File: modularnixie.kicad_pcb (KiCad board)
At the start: 2 copper layers, 69.8 x 21.6 mm, 37 parts, among them J1 Feed, J2 Feed, J3 HV, J4 HV, Q1 MMBT5551, Q10 MMBT5551, Q11 MMBT5551, Q12 MMBT5551, Q13 MMBT5551, Q14 MMBT5551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

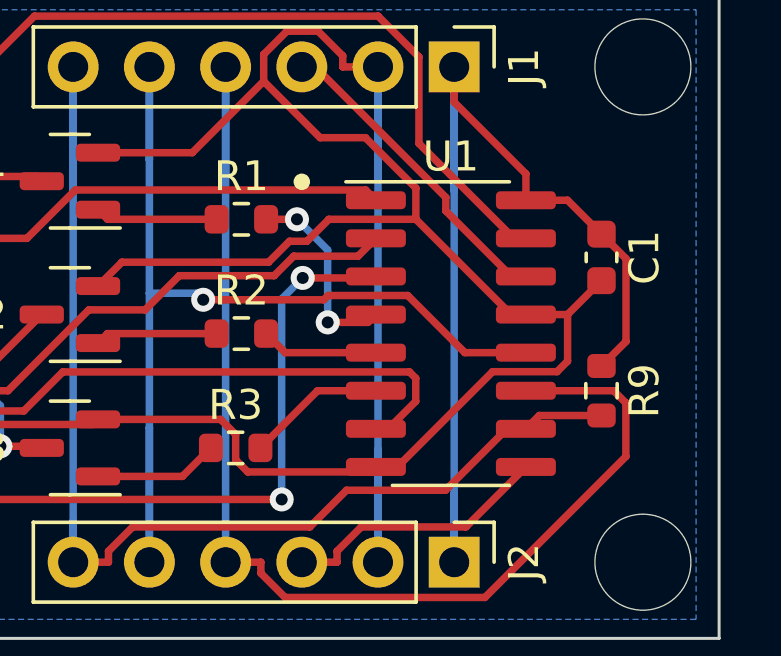
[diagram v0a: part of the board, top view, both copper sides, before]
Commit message: Actually replace SOP-16 with SOIC-16 to get 3D model
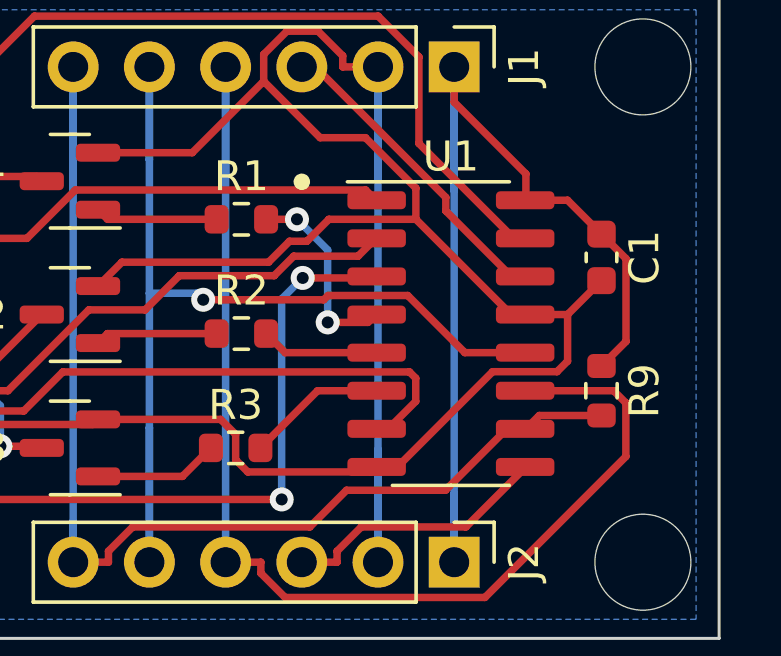
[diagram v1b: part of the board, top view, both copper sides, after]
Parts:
- U1: footprint Package_SO:SOP-16_3.9x9.9mm_P1.27mm -> Package_SO:SOIC-16_3.9x9.9mm_P1.27mm
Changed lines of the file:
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@@
     )
   )
-  (footprint "Package_SO:SOP-16_3.9x9.9mm_P1.27mm" (layer "F.Cu")
+  (footprint "Package_SO:SOIC-16_3.9x9.9mm_P1.27mm" (layer "F.Cu")
     (at 127.7172 64.135)
-    (descr "SOP, 16 Pin (https://www.diodes.com/assets/Datasheets/PAM8403.pdf), generated with kicad-footprint-generator ipc_gullwing_generator.py")
-    (tags "SOP SO")
+    (descr "SOIC, 16 Pin (JEDEC MS-012AC, https://www.analog.com/media/en/package-pcb-resources/package/pkg_pdf/soic_narrow-r/r_16.pdf), generated with kicad-footprint-generator ipc_gullwing_generator.py")
+    (tags "SOIC SO")
     (property "LCSC" "C5947")
     (property "Sheetfile" "modularnixie.kicad_sch")
@@
       (effects (font (size 0.98 0.98) (thickness 0.15)))
     )
+    (fp_line (start 0 -5.06) (end -3.45 -5.06) (layer "F.SilkS") (width 0.12))
+    (fp_line (start 0 5.06) (end 1.95 5.06) (layer "F.SilkS") (width 0.12))
+    (fp_line (start 0 -5.06) (end 1.95 -5.06) (layer "F.SilkS") (width 0.12))
     (fp_line (start 0 5.06) (end -1.95 5.06) (layer "F.SilkS") (width 0.12))
-    (fp_line (start 0 5.06) (end 1.95 5.06) (layer "F.SilkS") (width 0.12))
-    (fp_line (start 0 -5.06) (end -3.5 -5.06) (layer "F.SilkS") (width 0.12))
-    (fp_line (start 0 -5.06) (end 1.95 -5.06) (layer "F.SilkS") (width 0.12))
-    (fp_line (start -3.75 5.2) (end 3.75 5.2) (layer "F.CrtYd") (width 0.05))
-    (fp_line (start -3.75 -5.2) (end -3.75 5.2) (layer "F.CrtYd") (width 0.05))
-    (fp_line (start 3.75 -5.2) (end -3.75 -5.2) (layer "F.CrtYd") (width 0.05))
-    (fp_line (start 3.75 5.2) (end 3.75 -5.2) (layer "F.CrtYd") (width 0.05))
+    (fp_line (start 3.7 5.2) (end 3.7 -5.2) (layer "F.CrtYd") (width 0.05))
+    (fp_line (start -3.7 5.2) (end 3.7 5.2) (layer "F.CrtYd") (width 0.05))
+    (fp_line (start -3.7 -5.2) (end -3.7 5.2) (layer "F.CrtYd") (width 0.05))
+    (fp_line (start 3.7 -5.2) (end -3.7 -5.2) (layer "F.CrtYd") (width 0.05))
+    (fp_line (start 1.95 4.95) (end -1.95 4.95) (layer "F.Fab") (width 0.1))
+    (fp_line (start -0.975 -4.95) (end 1.95 -4.95) (layer "F.Fab") (width 0.1))
+    (fp_line (start -1.95 -3.975) (end -0.975 -4.95) (layer "F.Fab") (width 0.1))
+    (fp_line (start -1.95 4.95) (end -1.95 -3.975) (layer "F.Fab") (width 0.1))
     (fp_line (start 1.95 -4.95) (end 1.95 4.95) (layer "F.Fab") (width 0.1))
-    (fp_line (start -1.95 4.95) (end -1.95 -3.975) (layer "F.Fab") (width 0.1))
-    (fp_line (start -1.95 -3.975) (end -0.975 -4.95) (layer "F.Fab") (width 0.1))
-    (fp_line (start -0.975 -4.95) (end 1.95 -4.95) (layer "F.Fab") (width 0.1))
-    (fp_line (start 1.95 4.95) (end -1.95 4.95) (layer "F.Fab") (width 0.1))
-    (pad "1" smd roundrect (at -2.5 -4.445) (size 2 0.6) (layers "F.Cu" "F.Paste" "F.Mask") (roundrect_rratio 0.25)
+    (pad "1" smd roundrect (at -2.475 -4.445) (size 1.95 0.6) (layers "F.Cu" "F.Paste" "F.Mask") (roundrect_rratio 0.25)
       (net 34 "Net-(R11-Pad2)") (pinfunction "QB") (pintype "tri_state"))
-    (pad "2" smd roundrect (at -2.5 -3.175) (size 2 0.6) (layers "F.Cu" "F.Paste" "F.Mask") (roundrect_rratio 0.25)
+    (pad "2" smd roundrect (at -2.475 -3.175) (size 1.95 0.6) (layers "F.Cu" "F.Paste" "F.Mask") (roundrect_rratio 0.25)
       (net 35 "Net-(R12-Pad2)") (pinfunction "QC") (pintype "tri_state"))
-    (pad "3" smd roundrect (at -2.5 -1.905) (size 2 0.6) (layers "F.Cu" "F.Paste" "F.Mask") (roundrect_rratio 0.25)
+    (pad "3" smd roundrect (at -2.475 -1.905) (size 1.95 0.6) (layers "F.Cu" "F.Paste" "F.Mask") (roundrect_rratio 0.25)
       (net 36 "Net-(R13-Pad2)") (pinfunction "QD") (pintype "tri_state"))
-    (pad "4" smd roundrect (at -2.5 -0.635) (size 2 0.6) (layers "F.Cu" "F.Paste" "F.Mask") (roundrect_rratio 0.25)
+    (pad "4" smd roundrect (at -2.475 -0.635) (size 1.95 0.6) (layers "F.Cu" "F.Paste" "F.Mask") (roundrect_rratio 0.25)
       (net 30 "Net-(R1-Pad2)") (pinfunction "QE") (pintype "tri_state"))
-    (pad "5" smd roundrect (at -2.5 0.635) (size 2 0.6) (layers "F.Cu" "F.Paste" "F.Mask") (roundrect_rratio 0.25)
+    (pad "5" smd roundrect (at -2.475 0.635) (size 1.95 0.6) (layers "F.Cu" "F.Paste" "F.Mask") (roundrect_rratio 0.25)
       (net 31 "Net-(R2-Pad2)") (pinfunction "QF") (pintype "tri_state"))
-    (pad "6" smd roundrect (at -2.5 1.905) (size 2 0.6) (layers "F.Cu" "F.Paste" "F.Mask") (roundrect_rratio 0.25)
+    (pad "6" smd roundrect (at -2.475 1.905) (size 1.95 0.6) (layers "F.Cu" "F.Paste" "F.Mask") (roundrect_rratio 0.25)
       (net 32 "Net-(R3-Pad2)") (pinfunction "QG") (pintype "tri_state"))
-    (pad "7" smd roundrect (at -2.5 3.175) (size 2 0.6) (layers "F.Cu" "F.Paste" "F.Mask") (roundrect_rratio 0.25)
+    (pad "7" smd roundrect (at -2.475 3.175) (size 1.95 0.6) (layers "F.Cu" "F.Paste" "F.Mask") (roundrect_rratio 0.25)
       (net 39 "Net-(R4-Pad2)") (pinfunction "QH") (pintype "tri_state"))
-    (pad "8" smd roundrect (at -2.5 4.445) (size 2 0.6) (layers "F.Cu" "F.Paste" "F.Mask") (roundrect_rratio 0.25)
+    (pad "8" smd roundrect (at -2.475 4.445) (size 1.95 0.6) (layers "F.Cu" "F.Paste" "F.Mask") (roundrect_rratio 0.25)
       (net 2 "GND") (pinfunction "GND") (pintype "power_in"))
-    (pad "9" smd roundrect (at 2.5 4.445) (size 2 0.6) (layers "F.Cu" "F.Paste" "F.Mask") (roundrect_rratio 0.25)
+    (pad "9" smd roundrect (at 2.475 4.445) (size 1.95 0.6) (layers "F.Cu" "F.Paste" "F.Mask") (roundrect_rratio 0.25)
       (net 7 "Net-(J2-Pad3)") (pinfunction "QH'") (pintype "output"))
-    (pad "10" smd roundrect (at 2.5 3.175) (size 2 0.6) (layers "F.Cu" "F.Paste" "F.Mask") (roundrect_rratio 0.25)
+    (pad "10" smd roundrect (at 2.475 3.175) (size 1.95 0.6) (layers "F.Cu" "F.Paste" "F.Mask") (roundrect_rratio 0.25)
       (net 3 "Net-(J1-Pad6)") (pinfunction "~{SRCLR}") (pintype "input"))
-    (pad "11" smd roundrect (at 2.5 1.905) (size 2 0.6) (layers "F.Cu" "F.Paste" "F.Mask") (roundrect_rratio 0.25)
+    (pad "11" smd roundrect (at 2.475 1.905) (size 1.95 0.6) (layers "F.Cu" "F.Paste" "F.Mask") (roundrect_rratio 0.25)
       (net 5 "Net-(J1-Pad4)") (pinfunction "SRCLK") (pintype "input"))
-    (pad "12" smd roundrect (at 2.5 0.635) (size 2 0.6) (layers "F.Cu" "F.Paste" "F.Mask") (roundrect_rratio 0.25)
+    (pad "12" smd roundrect (at 2.475 0.635) (size 1.95 0.6) (layers "F.Cu" "F.Paste" "F.Mask") (roundrect_rratio 0.25)
       (net 6 "Net-(J1-Pad5)") (pinfunction "RCLK") (pintype "input"))
-    (pad "13" smd roundrect (at 2.5 -0.635) (size 2 0.6) (layers "F.Cu" "F.Paste" "F.Mask") (roundrect_rratio 0.25)
+    (pad "13" smd roundrect (at 2.475 -0.635) (size 1.95 0.6) (layers "F.Cu" "F.Paste" "F.Mask") (roundrect_rratio 0.25)
       (net 2 "GND") (pinfunction "~{OE}") (pintype "input"))
-    (pad "14" smd roundrect (at 2.5 -1.905) (size 2 0.6) (layers "F.Cu" "F.Paste" "F.Mask") (roundrect_rratio 0.25)
+    (pad "14" smd roundrect (at 2.475 -1.905) (size 1.95 0.6) (layers "F.Cu" "F.Paste" "F.Mask") (roundrect_rratio 0.25)
       (net 4 "Net-(J1-Pad3)") (pinfunction "SER") (pintype "input"))
-    (pad "15" smd roundrect (at 2.5 -3.175) (size 2 0.6) (layers "F.Cu" "F.Paste" "F.Mask") (roundrect_rratio 0.25)
+    (pad "15" smd roundrect (at 2.475 -3.175) (size 1.95 0.6) (layers "F.Cu" "F.Paste" "F.Mask") (roundrect_rratio 0.25)
       (net 33 "Net-(R10-Pad2)") (pinfunction "QA") (pintype "tri_state"))
-    (pad "16" smd roundrect (at 2.5 -4.445) (size 2 0.6) (layers "F.Cu" "F.Paste" "F.Mask") (roundrect_rratio 0.25)
+    (pad "16" smd roundrect (at 2.475 -4.445) (size 1.95 0.6) (layers "F.Cu" "F.Paste" "F.Mask") (roundrect_rratio 0.25)
       (net 1 "VCC") (pinfunction "VCC") (pintype "power_in"))
-    (model "${KICAD6_3DMODEL_DIR}/Package_SO.3dshapes/SOP-16_3.9x9.9mm_P1.27mm.wrl"
+    (model "${KICAD6_3DMODEL_DIR}/Package_SO.3dshapes/SOIC-16_3.9x9.9mm_P1.27mm.wrl"
       (offset (xyz 0 0 0))
       (scale (xyz 1 1 1))
